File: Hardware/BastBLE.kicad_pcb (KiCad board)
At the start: 2 copper layers, 50.8 x 22.9 mm, 39 parts, among them J1 Conn_Battery, J2 SWD, J3 Conn_left, J4 Conn_right, P1 USB_C_Plug_USB2.0, Q1 DMG3415U-7, SW1 RESET, U1 AP2112K-3.3, U2 E73-2G4M08S1C, U3 MCP73831-2-OT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

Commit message: Routeo a4 a5, fix sck mosi
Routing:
- net /A4: track 0.00 -> 33.3 mm, vias 0 -> 1
- net /A5: track 0.00 -> 27.2 mm, vias 0 -> 1
- net /LED: track 13.2 -> 0.00 mm
- net /SCK: track 31.7 -> 29.3 mm
- net Net-(D2-Pad2): track 1.56 -> 0.00 mm
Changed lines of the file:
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@@
     (thickness 1.6)
     (drawings 14)
-    (tracks 211)
+    (tracks 219)
     (zones 0)
     (modules 39)
@@
   (segment (start 176.522 98.826998) (end 176.522 97.201) (width 0.3) (layer B.Cu) (net 7))
   (segment (start 173.678999 101.669999) (end 176.522 98.826998) (width 0.3) (layer B.Cu) (net 7))
-  (segment (start 157.829999 101.949999) (end 157.829999 86.270001) (width 0.3) (layer B.Cu) (net 8))
+  (segment (start 157.829999 88.725167) (end 158.703167 87.851999) (width 0.3) (layer B.Cu) (net 8))
+  (segment (start 158.703167 87.851999) (end 166.935014 87.851999) (width 0.3) (layer B.Cu) (net 8))
   (segment (start 158.75 102.87) (end 157.829999 101.949999) (width 0.3) (layer B.Cu) (net 8))
-  (segment (start 157.829999 86.270001) (end 159.2 84.9) (width 0.3) (layer B.Cu) (net 8))
-  (via (at 170.65 84.9) (size 0.8) (drill 0.4) (layers F.Cu B.Cu) (net 8))
-  (segment (start 159.2 84.9) (end 170.65 84.9) (width 0.3) (layer B.Cu) (net 8))
-  (segment (start 170.65 86.211) (end 170.68 86.241) (width 0.3) (layer F.Cu) (net 8))
-  (segment (start 170.65 84.9) (end 170.65 86.211) (width 0.3) (layer F.Cu) (net 8))
+  (segment (start 157.829999 101.949999) (end 157.829999 88.725167) (width 0.3) (layer B.Cu) (net 8))
+  (via (at 170.68 87.83) (size 0.8) (drill 0.4) (layers F.Cu B.Cu) (net 8))
+  (segment (start 170.658001 87.851999) (end 170.68 87.83) (width 0.3) (layer B.Cu) (net 8))
+  (segment (start 166.935014 87.851999) (end 170.658001 87.851999) (width 0.3) (layer B.Cu) (net 8))
+  (segment (start 170.68 87.83) (end 170.68 86.241) (width 0.3) (layer F.Cu) (net 8))
+  (via (at 168.14 87.101989) (size 0.8) (drill 0.4) (layers F.Cu B.Cu) (net 9))
+  (segment (start 168.14 86.241) (end 168.14 87.101989) (width 0.3) (layer F.Cu) (net 9))
+  (segment (start 156.21 89.371084) (end 158.479095 87.101989) (width 0.3) (layer B.Cu) (net 9))
+  (segment (start 167.574315 87.101989) (end 168.14 87.101989) (width 0.3) (layer B.Cu) (net 9))
+  (segment (start 158.479095 87.101989) (end 167.574315 87.101989) (width 0.3) (layer B.Cu) (net 9))
+  (segment (start 156.21 102.87) (end 156.21 89.371084) (width 0.3) (layer B.Cu) (net 9))
+  (via (at 173.22 86.241) (size 0.8) (drill 0.4) (layers F.Cu B.Cu) (net 10))
+  (segment (start 173.22 86.241) (end 158.632962 86.241) (width 0.3) (layer B.Cu) (net 10))
+  (segment (start 158.632962 86.241) (end 153.67 91.203962) (width 0.3) (layer B.Cu) (net 10))
+  (segment (start 153.67 101.667919) (end 153.67 102.87) (width 0.3) (layer B.Cu) (net 10))
+  (segment (start 153.67 91.203962) (end 153.67 101.667919) (width 0.3) (layer B.Cu) (net 10))
   (segment (start 165.977887 97.592113) (end 164.731011 97.592113) (width 0.3) (layer F.Cu) (net 13))
   (segment (start 161.904988 97.955012) (end 158.190001 101.669999) (width 0.3) (layer F.Cu) (net 13))
@@
   (segment (start 159.13 96.79) (end 160.48 96.79) (width 0.5) (layer B.Cu) (net 15))
   (via (at 161.359968 95.751247) (size 0.8) (drill 0.4) (layers F.Cu B.Cu) (net 15))
-  (segment (start 162.13 85.11) (end 160.565 85.11) (width 0.3) (layer F.Cu) (net 21))
   (segment (start 140.245 96.62) (end 140.255 96.61) (width 0.3) (layer F.Cu) (net 22))
   (segment (start 138.685 96.62) (end 140.245 96.62) (width 0.3) (layer F.Cu) (net 22))
@@
   (segment (start 142.025 91.255) (end 140.73 92.55) (width 0.3) (layer F.Cu) (net 23))
   (segment (start 142.025 90.65) (end 142.025 91.255) (width 0.3) (layer F.Cu) (net 23))
-  (segment (start 164.840001 84.149999) (end 173.843999 84.149999) (width 0.3) (layer F.Cu) (net 24))
-  (segment (start 173.843999 84.149999) (end 175.76 86.066) (width 0.3) (layer F.Cu) (net 24))
-  (segment (start 163.88 85.11) (end 164.840001 84.149999) (width 0.3) (layer F.Cu) (net 24))
-  (segment (start 175.76 86.066) (end 175.76 86.241) (width 0.3) (layer F.Cu) (net 24))
   (segment (start 155.77 89.015) (end 155.575 88.82) (width 0.5) (layer F.Cu) (net 25))
   (segment (start 155.77 90.465) (end 155.77 89.015) (width 0.5) (layer F.Cu) (net 25))
@@
   (segment (start 161.89 89.16) (end 163.381 89.16) (width 0.3) (layer F.Cu) (net 45))
   (segment (start 161.02 90.03) (end 161.89 89.16) (width 0.3) (layer F.Cu) (net 45))
-  (segment (start 163.381 96.78) (end 159.151 96.78) (width 0.3) (layer F.Cu) (net 47))
-  (segment (start 158.995072 96.624072) (end 158.496 96.125) (width 0.3) (layer F.Cu) (net 47))
-  (segment (start 159.151 96.78) (end 158.995072 96.624072) (width 0.3) (layer F.Cu) (net 47))
+  (segment (start 158.496 96.125) (end 160.355 96.125) (width 0.3) (layer F.Cu) (net 47))
+  (segment (start 160.355 96.125) (end 161.01 96.78) (width 0.3) (layer F.Cu) (net 47))
+  (segment (start 161.01 96.78) (end 161.48 96.78) (width 0.3) (layer F.Cu) (net 47))
+  (segment (start 163.381 96.78) (end 161.48 96.78) (width 0.3) (layer F.Cu) (net 47))
   (zone (net 2) (net_name GND) (layer F.Cu) (hatch edge 0.508)
     (connect_pads (clearance 0.508))

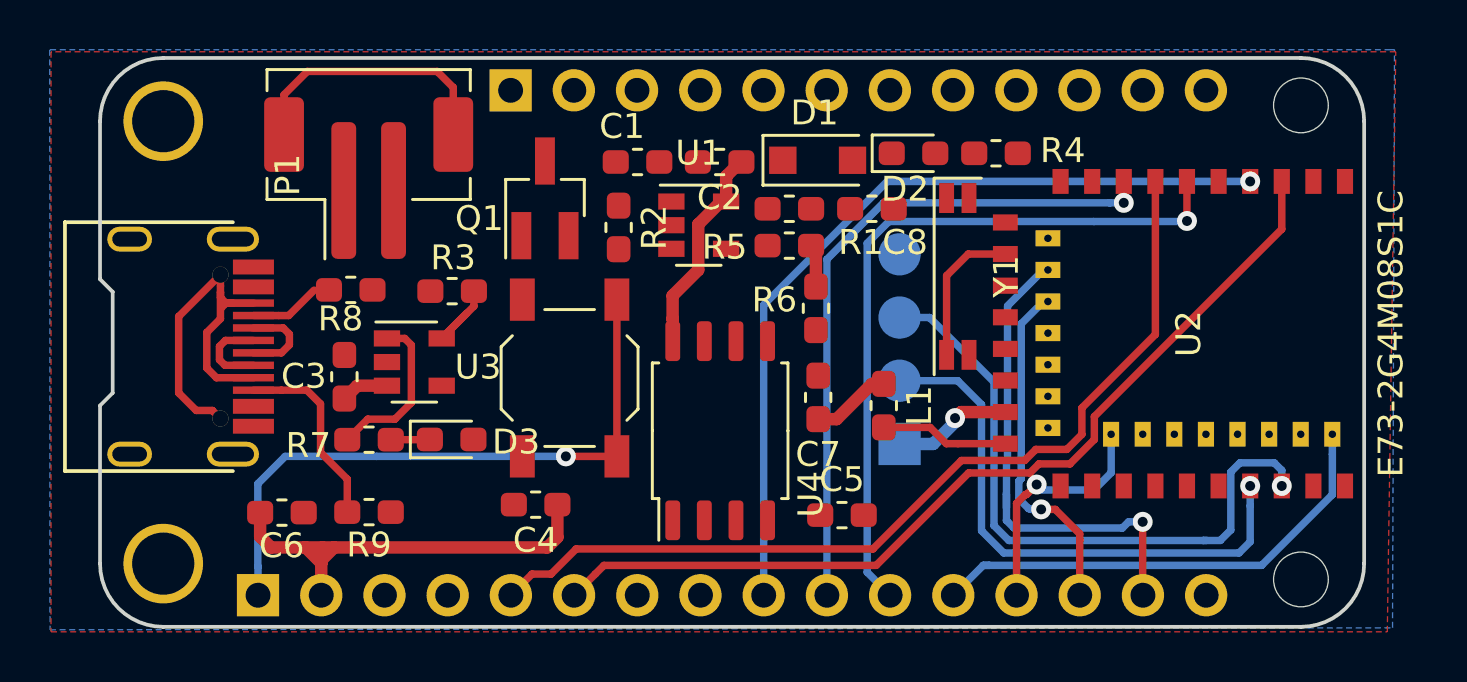
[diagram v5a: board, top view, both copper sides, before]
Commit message: fix c8, r6, and pin
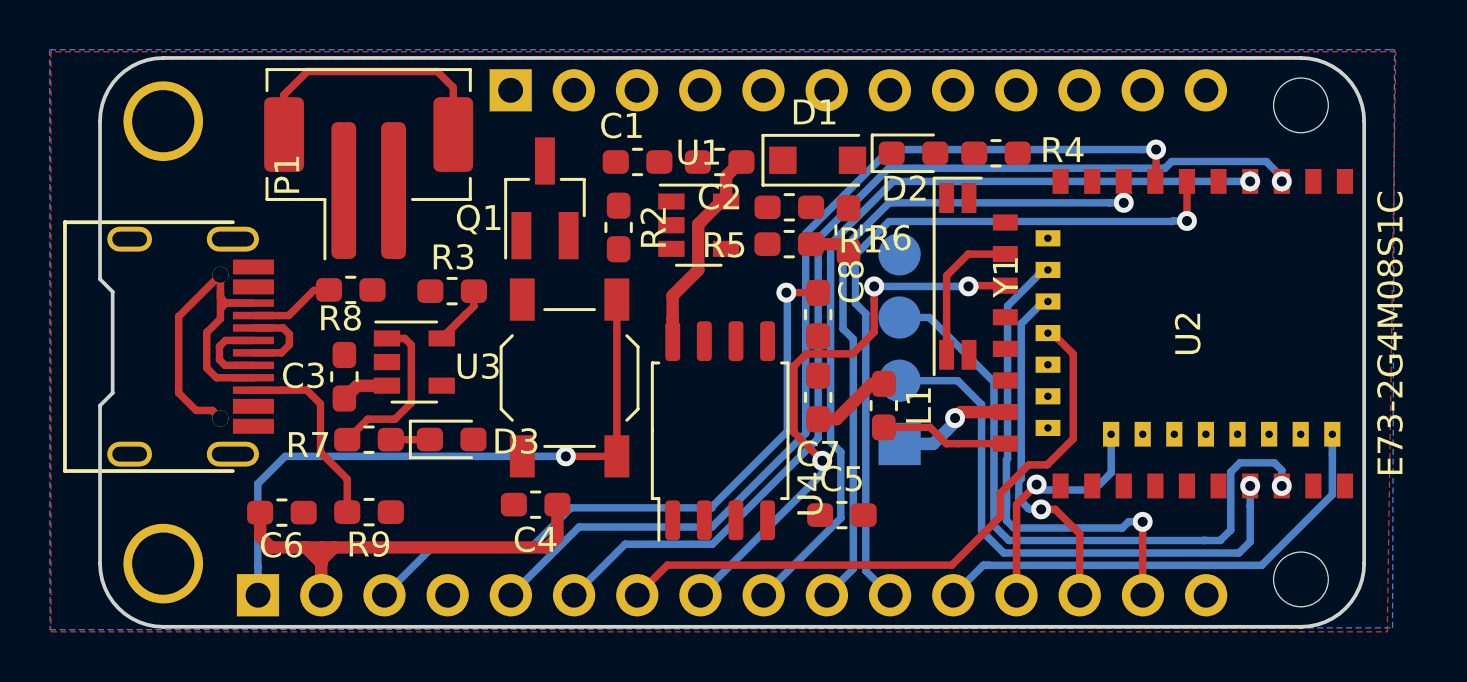
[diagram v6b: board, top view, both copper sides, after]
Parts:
- moved C8 4.77 mm to (155.9, 91.6), turned to 270 degrees
- moved R6 3.41 mm to (157.1, 88.2), turned to 90 degrees
- moved R5 0.06 mm to (154.7, 88.8)
- moved R1 0.06 mm to (154.7, 87.3)
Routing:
- net /AREF: track 0.00 -> 25.8 mm, vias 0 -> 1
- net /A2: track 0.00 -> 25.4 mm
- net /A3: track 0.00 -> 22.6 mm, vias 0 -> 3
- net /A1: track 37.0 -> 40.8 mm, vias 0 -> 1
- net /A0: track 37.0 -> 39.3 mm, vias 0 -> 1

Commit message: D11-SDA
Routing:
- net /D9: track 0.00 -> 28.1 mm
- net /SDA: track 0.00 -> 26.4 mm, vias 0 -> 1
- net /D6: track 0.00 -> 25.9 mm, vias 0 -> 1
- net /SCL: track 0.00 -> 21.9 mm
- net /D5: track 0.00 -> 14.2 mm, vias 0 -> 1
- net /A4: track 33.5 -> 36.3 mm
- net /A1: track 40.8 -> 43.3 mm
- net /A0: track 39.3 -> 38.1 mm
- net /SWCLK: track 26.0 -> 27.1 mm

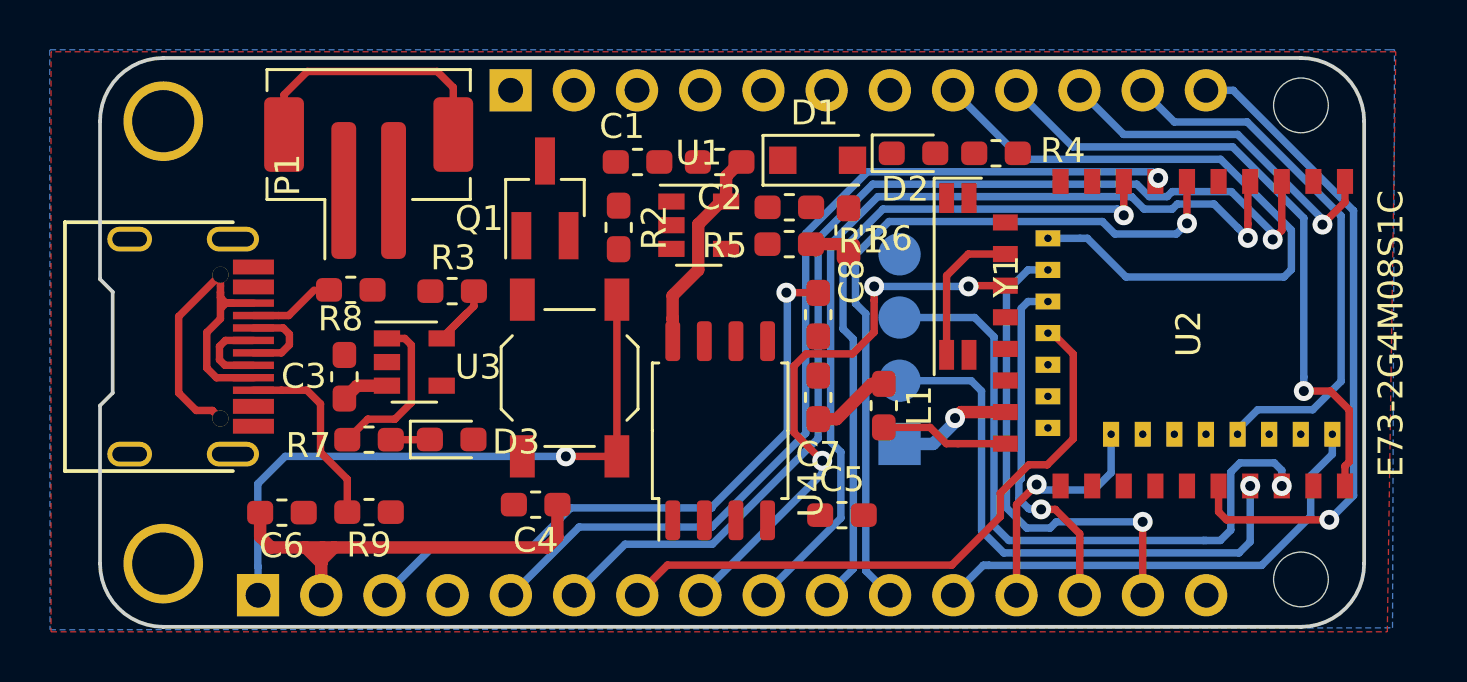
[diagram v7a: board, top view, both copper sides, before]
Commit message: change pins schematic
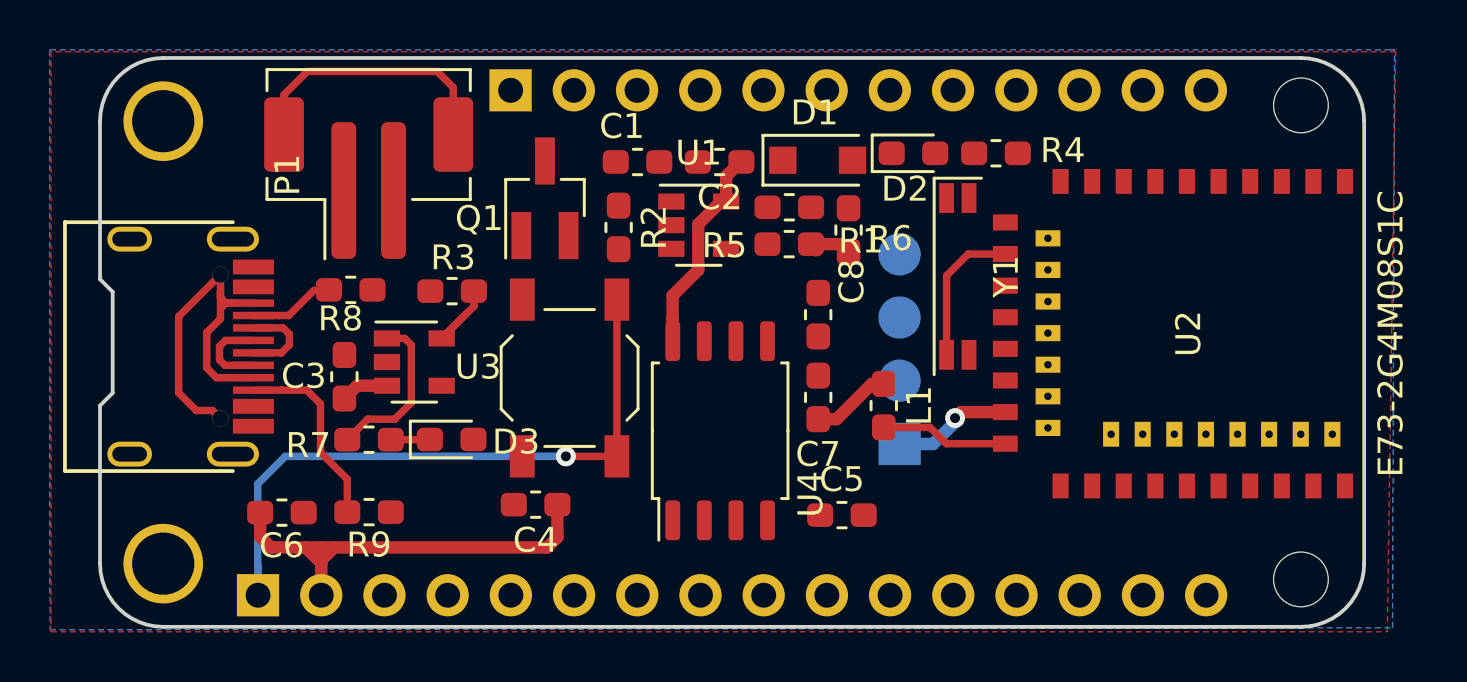
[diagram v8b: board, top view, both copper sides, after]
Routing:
- net /A1: track 43.3 -> 0.00 mm, vias 1 -> 0
- net /A0: track 38.1 -> 0.00 mm, vias 1 -> 0
- net /A4: track 36.3 -> 0.00 mm, vias 1 -> 0
- net /SCK: track 30.2 -> 0.00 mm, vias 1 -> 0
- net /D9: track 28.1 -> 0.00 mm
- net /A5: track 27.9 -> 0.00 mm, vias 1 -> 0
- net /SWCLK: track 27.1 -> 0.00 mm, vias 1 -> 0
- net /SDA: track 26.4 -> 0.00 mm, vias 1 -> 0
- net /D6: track 25.9 -> 0.00 mm, vias 1 -> 0
- net /AREF: track 25.8 -> 0.00 mm, vias 1 -> 0
- net /A2: track 25.4 -> 0.00 mm
- net /SWDIO: track 22.7 -> 0.00 mm, vias 1 -> 0
- net /A3: track 22.6 -> 0.00 mm, vias 3 -> 0
- net /SCL: track 21.9 -> 0.00 mm
- net /TX: track 19.6 -> 0.00 mm, vias 1 -> 0
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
